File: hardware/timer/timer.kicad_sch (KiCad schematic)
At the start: 18 parts, among them J1 JST_XH_HOST_UART, U1 Pico, U2 TM1637

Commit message: タイマー基板: 実フットプリント化・電池入力(J6/Q1/R5)追加・Pico 40ピン化・配線
- PCBを実ライブラリのフットプリントで作り直し、以後KiCadで手編集(tools/に一回限りのスクリプト)
- 回路図のFootprintフィールドを補完、C3を8mm缶に変更
- Pico専用フットプリント RPi_Pico_TH_Headers(THT40ピンのみ、浮き実装、3D +2.5mm)と40ピンシンボル
- 電池入力 J6 -> Q1(逆接続保護) -> +5V。F6は廃止(保護は電池箱側)
- 未解決(作業途中): DRCのstarved_thermal 4件、回路図とのパリティ差分(基板更新で解消見込み)

Co-Authored-By: Claude Sonnet 5.5 <noreply@anthropic.com>
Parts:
- removed F1: MF-R185 (1.85A hold / 3.7A trip @23C, Akizuki 112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, symbol Device:Fuse
- removed JP1: TM1637_VDD_SEL, Connector_PinHeader_2.54mm:PinHeader_1x03_P2.54mm_Vertical, symbol Connector_Generic:Conn_01x03
- added F1, F2, F3, F4, F5: Polyfuse_Small, Timer_Local:MF-RX030_Radial_P5.10mm, symbol Device:Polyfuse_Small
- added J2, J3, J4, J5, J7: Conn_01x04, Connector_JST:JST_XH_B4B-XH-A_1x04_P2.50mm_Vertical, symbol Connector_Generic:Conn_01x04
- added J6: Conn_01x02, Connector_JST:JST_XH_B2B-XH-A_1x02_P2.50mm_Vertical, symbol Connector_Generic:Conn_01x02
- added J8: Conn_01x03, Connector_JST:JST_XH_B3B-XH-A_1x03_P2.50mm_Vertical, symbol Connector_Generic:Conn_01x03
- added Q1: IRLML6402, Package_TO_SOT_SMD:SOT-23, symbol Transistor_FET:IRLML6402
- added R3, R4, R5: R, Resistor_THT:R_Axial_DIN0207_L6.3mm_D2.5mm_P2.54mm_Vertical, symbol Device:R
- added U3: Pico, Timer_Local:RPi_Pico_TH_Headers, symbol Timer_Local:Pico_TH40
- C1: value 100nF -> C
- C2: value 100uF -> C_Polarized
- C3: value 100uF -> C_Polarized; footprint Capacitor_THT:CP_Radial_D5.0mm_P2.00mm -> Capacitor_THT:CP_Radial_D8.0mm_P3.50mm
- D1: value LED (colon, top) -> LED
- D2: value LED (colon, bottom) -> LED
- D3: value LED (strike 1) -> LED
- D4: value LED (strike 2) -> LED
- J1: value JST_XH_HOST_UART -> Conn_01x04
- R1, R2: value 330 -> R
- U1: footprint RPi_Pico:RPi_Pico_SMD_TH -> Timer_Local:RPi_Pico_TH_Headers; symbol RPi_Pico:Pico -> Timer_Local:Pico_TH40
- U2: footprint (none) -> Package_DIP:DIP-20_W7.62mm
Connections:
- net TM_VDD is gone; now on net +5V: C1.1, C2.1, U2.16 (VDD)
- net +5V: now also C3.1, F1.1, F2.1, F3.1, F4.1, F5.1, Q1.2 (S), U3.39 (VSYS)
- net GND: now also J2.4 (Pin_4), J3.4 (Pin_4), J4.4 (Pin_4), J5.4 (Pin_4), J6.2 (Pin_2), J7.4 (Pin_4), J8.1 (Pin_1), R5.2, U3.13 (GND), U3.18 (GND), U3.23 (GND), U3.28 (GND), U3.3 (GND), U3.33 (AGND), U3.38 (GND), U3.8 (GND); no longer U1.42 (GND)
- net J1_5V renamed VCC_J1
- net VCC_J1: now also F1.2; no longer C3.1
- net UART_RX renamed M_TX
- net M_TX: now also U3.24 (GPIO18); no longer J1.2 (Pin_2)
- net UART_TX renamed M_RX
- net M_RX: now also U3.25 (GPIO19); no longer J1.1 (Pin_1)
- new net: Q1.1 (G), R5.1
- new net +3V3_H: J7.3 (Pin_3), R3.1, R4.1, U3.36 (3V3)
- new net S1_RX: J1.1 (Pin_1), U3.12 (GPIO9)
- new net S1_TX: J1.2 (Pin_2), U3.11 (GPIO8)
- new net S2_RX: J2.1 (Pin_1), U3.17 (GPIO13)
- new net S2_TX: J2.2 (Pin_2), U3.16 (GPIO12)
- new net S3_RX: J3.1 (Pin_1), U3.15 (GPIO11)
- new net S3_TX: J3.2 (Pin_2), U3.14 (GPIO10)
- new net S4_RX: J4.1 (Pin_1), U3.20 (GPIO15)
- new net S4_TX: J4.2 (Pin_2), U3.19 (GPIO14)
- new net S5_RX: J5.1 (Pin_1), U3.22 (GPIO17)
- new net S5_TX: J5.2 (Pin_2), U3.21 (GPIO16)
- new net SCL: J7.2 (Pin_2), R4.2, U3.2 (GPIO1)
- new net SDA: J7.1 (Pin_1), R3.2, U3.1 (GPIO0)
- new net SHARED_ODDEVEN: J8.2 (Pin_2), U3.4 (GPIO2)
- new net SHARED_VOWEL: J8.3 (Pin_3), U3.5 (GPIO3)
- new net VCC_J2: F2.2, J2.3 (Pin_3)
- new net VCC_J3: F3.2, J3.3 (Pin_3)
- new net VCC_J4: F4.2, J4.3 (Pin_3)
- new net VCC_J5: F5.2, J5.3 (Pin_3)
- new net VIN_5V: J6.1 (Pin_1), Q1.3 (D)
- no-connect marks 28 -> 40
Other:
- note added: "5V IN ONLY (J6 = regulated 5V from the battery-box DC-DC, never raw battery voltage) J6 pin1 = +5V, pin2 = GND -> Q1 reverse-polarity guard -> +5V rail (no fuse: F6 removed 2026-09-30) USB rule: unplug J6 before flashing over USB (Q1 conducts both ways when the rail is up). USB-only (J6 empty) is for bench tests only"
- title: Timer / strike-count display module -> Timer + host board (2x Pico 2, 80x80mm)

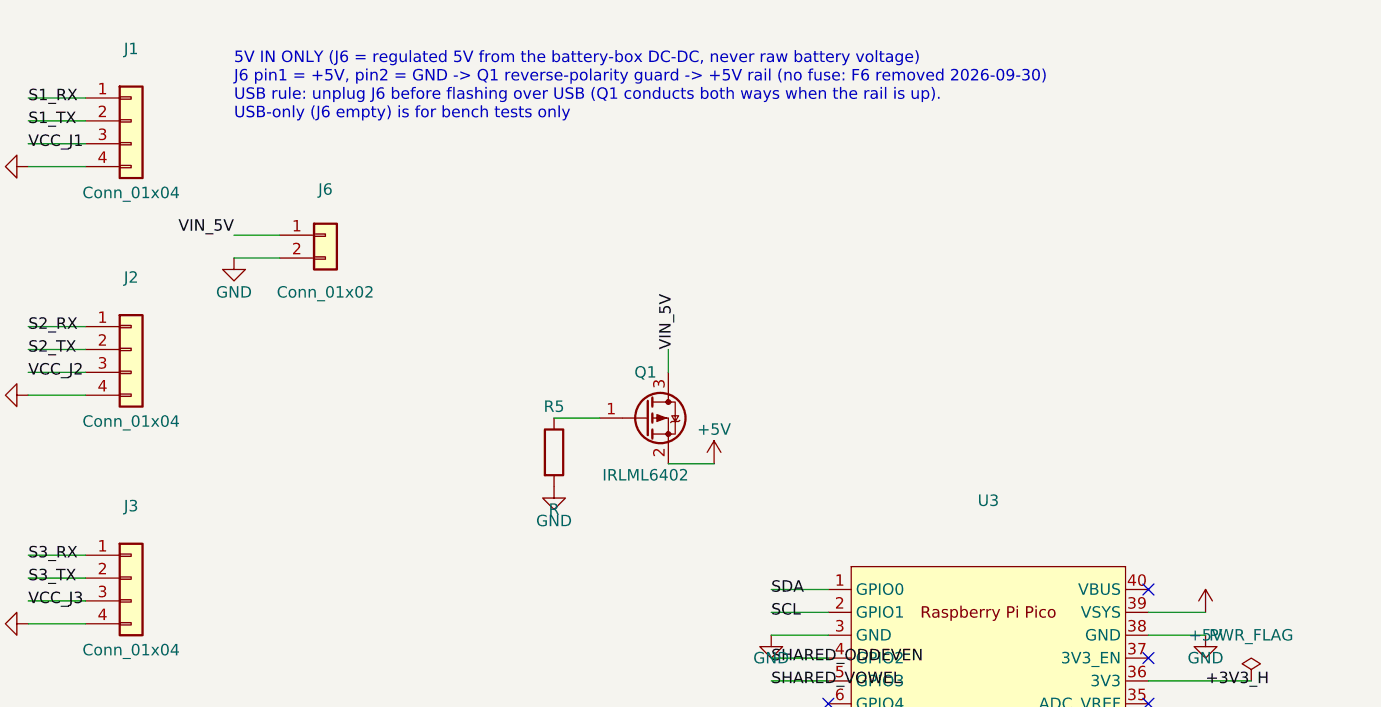
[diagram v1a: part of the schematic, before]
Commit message: タイマー基板: 電池入力にDC-DC(AE-TPS63802)を追加、F6復活、共有ライブラリ(shared_lib)
- 電池(単3x3)J6 -> F6 -> Q1(逆接続保護) -> AE-TPS63802(昇降圧) -> +5V
- Timer_Local に AE-TPS63802 のシンボル/フットプリントを追加
- hardware/shared_lib: OSC_Shared(Pico_TH40、RPi_Pico_TH_Headers)と適用スクリプト
- 回路図とPCBのパリティ0

作業途中(未解決): DRCのitems_not_allowed 7件(+5V/VBAT_Fの配線端点が隅12mm角に入る)、starved_thermal 10件

Co-Authored-By: Claude Sonnet 5.5 <noreply@anthropic.com>
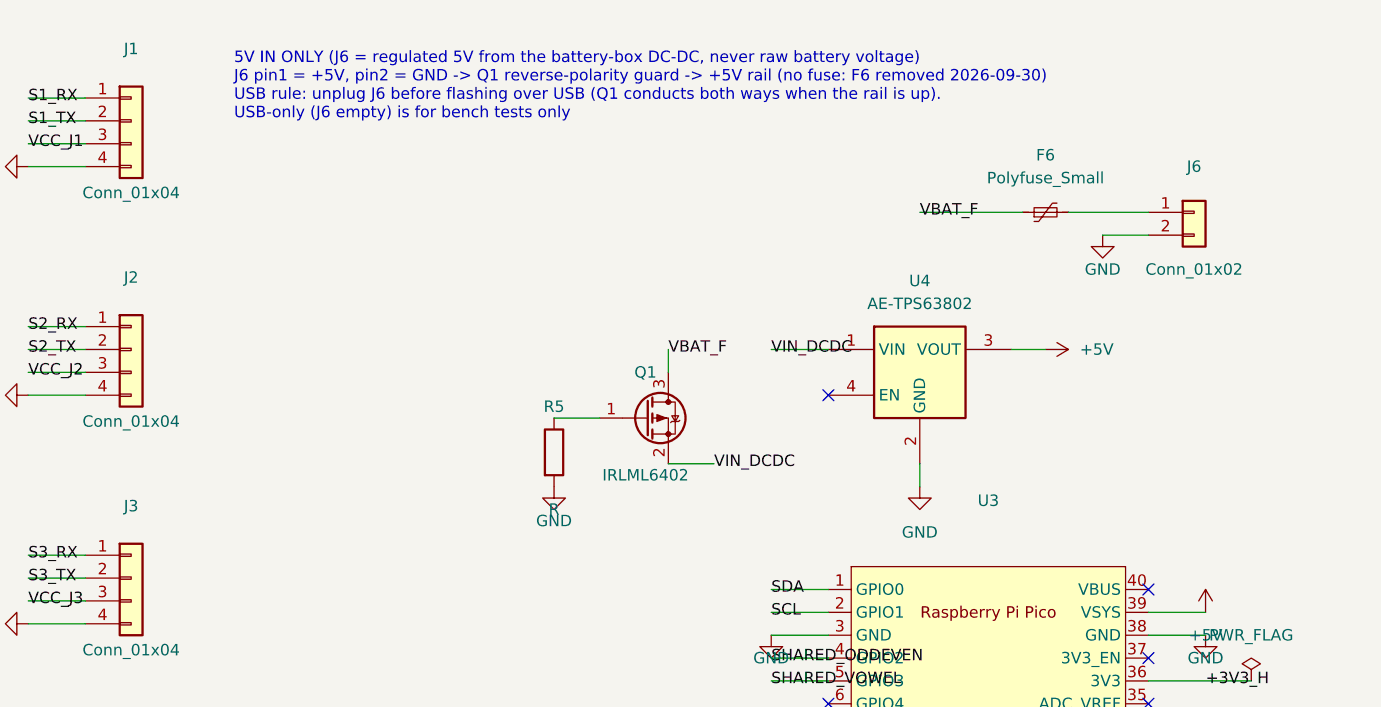
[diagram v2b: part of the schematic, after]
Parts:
- added F6: Polyfuse_Small, Timer_Local:MF-R185_Radial_P5.10mm, symbol Device:Polyfuse_Small
- added U4: AE-TPS63802, Timer_Local:AE-TPS63802, symbol Timer_Local:AE-TPS63802
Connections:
- net +5V: now also U4.3 (VOUT); no longer Q1.2 (S)
- net GND: now also U4.2 (GND)
- net VIN_5V: no longer names the net of J6.1 (Pin_1)
- net VIN_5V: now also F6.2; no longer Q1.3 (D)
- new net VBAT_F: F6.1, Q1.3 (D)
- new net VIN_DCDC: Q1.2 (S), U4.1 (VIN)
- no-connect marks 40 -> 41
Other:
- moved on the sheet: J6
